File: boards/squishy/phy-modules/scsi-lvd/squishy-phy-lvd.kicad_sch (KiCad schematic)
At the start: 39 parts, among them J1 SCSI PHY Mezz, J2 SCSI Connector, J3 Conn_01x04, Q5 PMDPB58UPE,115, Q6 DMN65D8L-7, U1 M24C02-RMC, U21 LM321, U39 LM2903

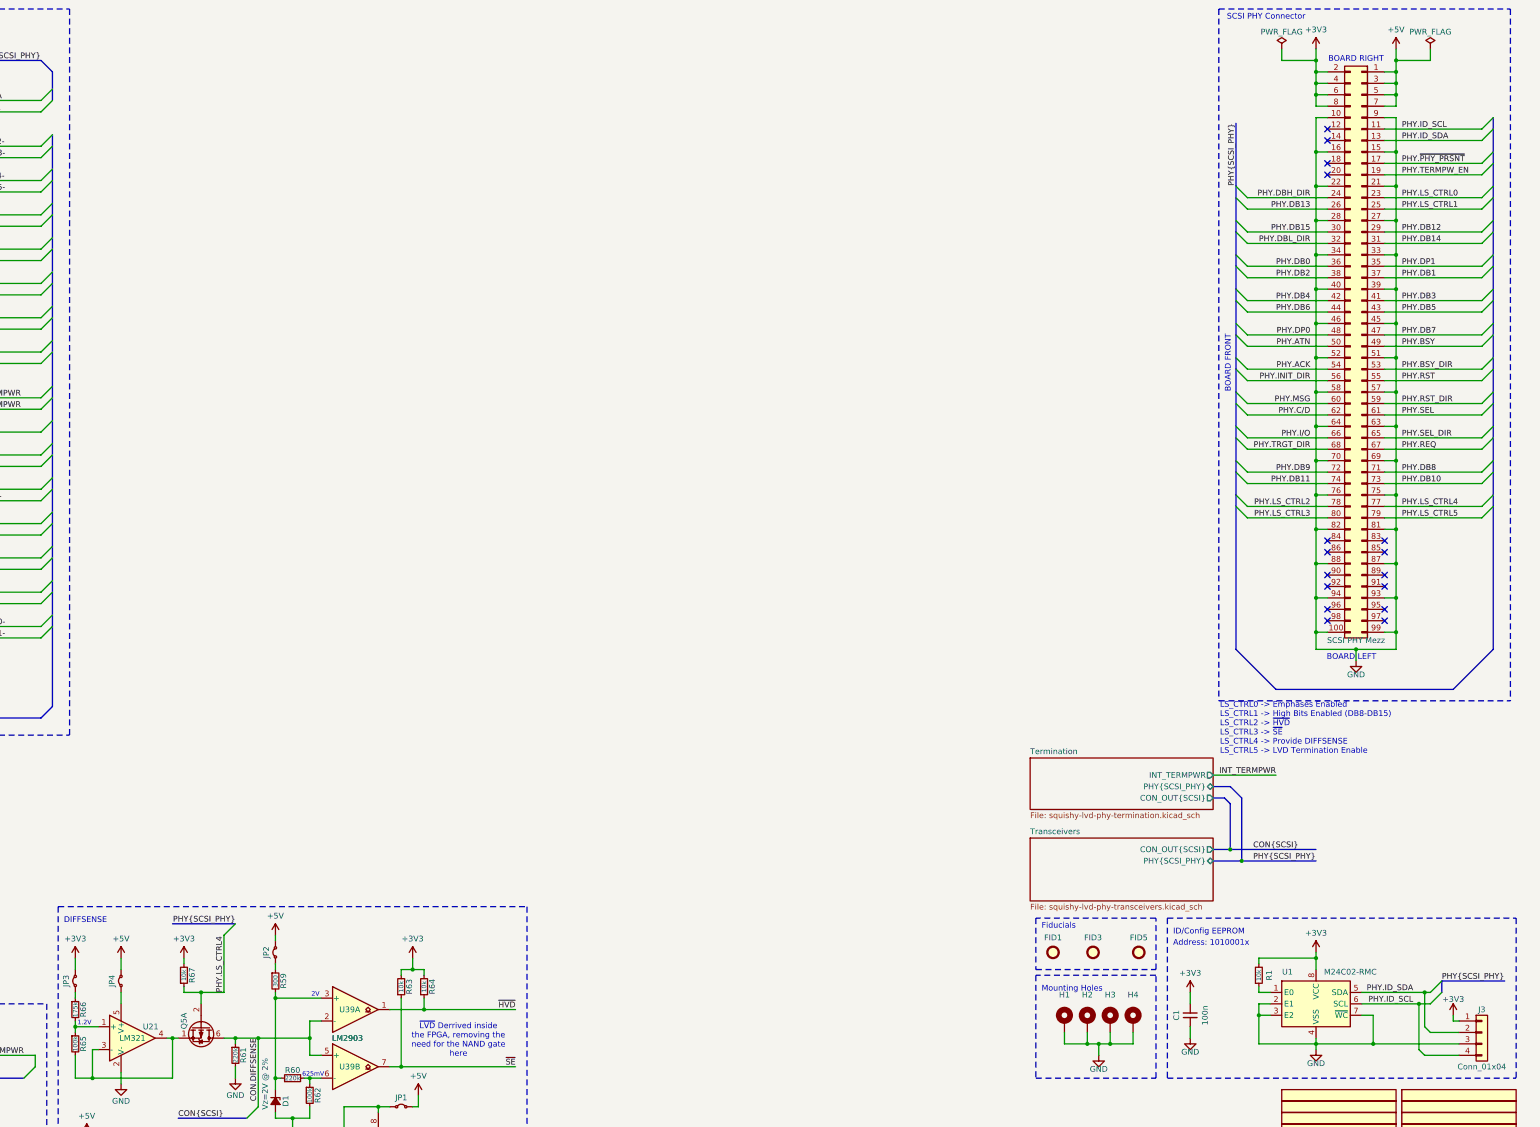
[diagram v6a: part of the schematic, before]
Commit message: squishy: phy: lvd: Started re-working the LVD PHY
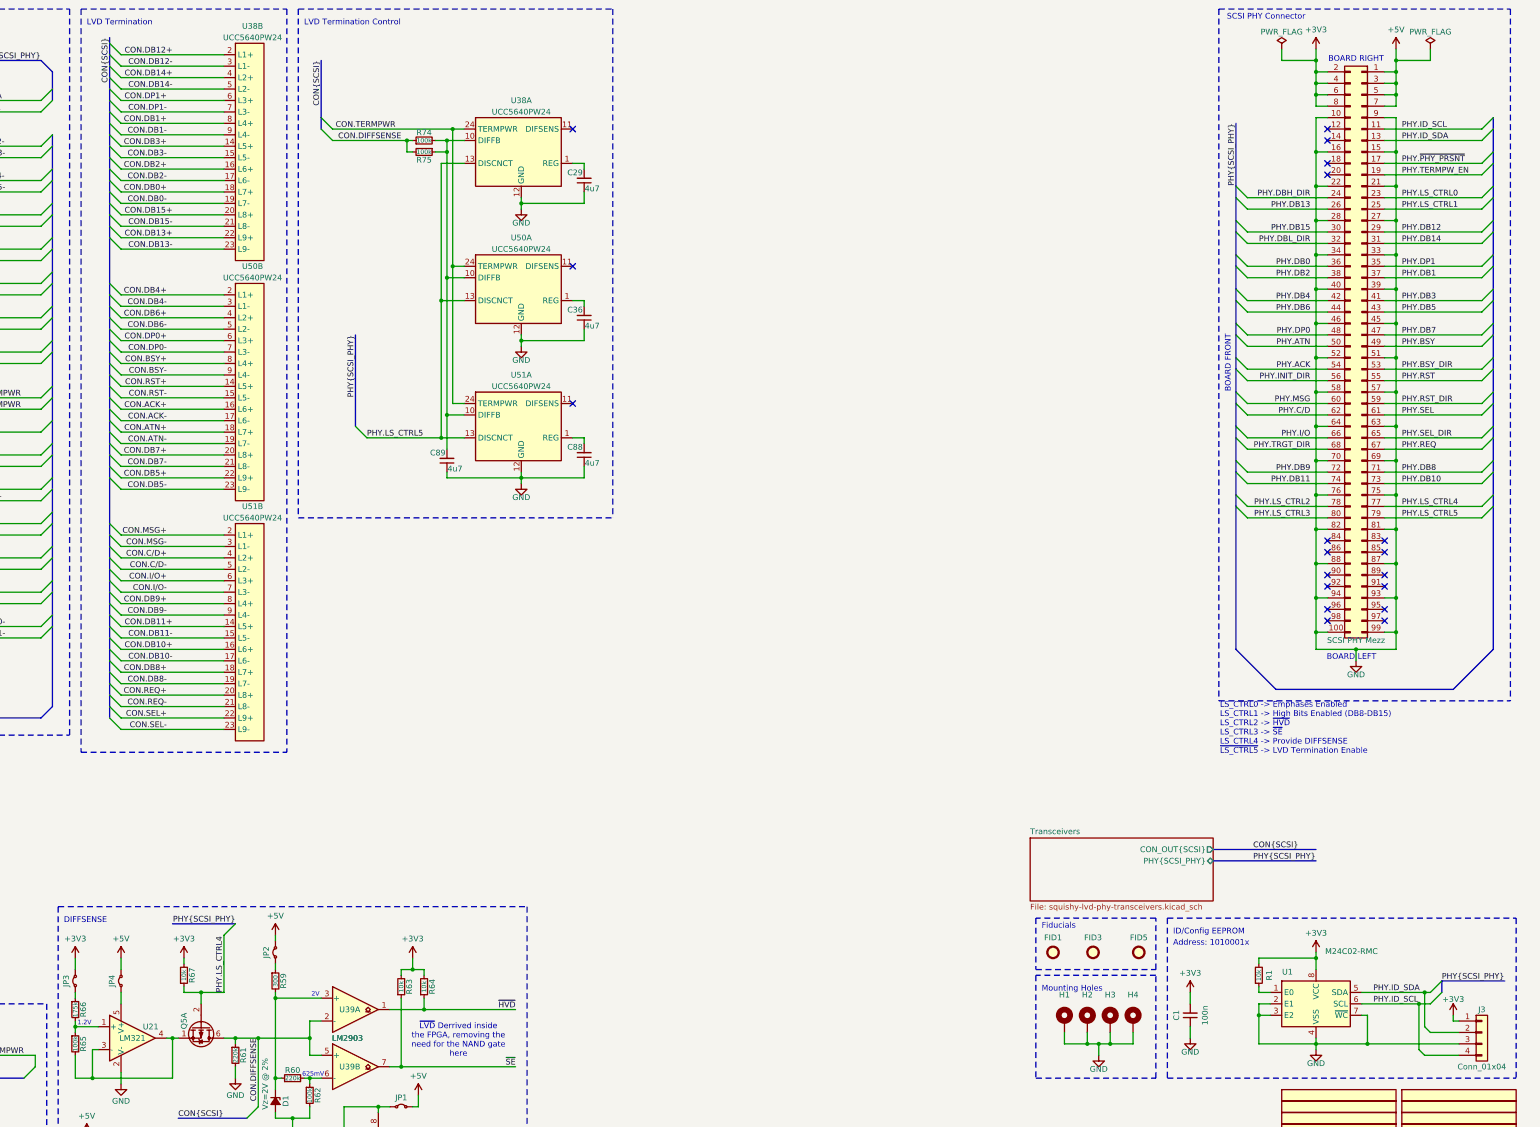
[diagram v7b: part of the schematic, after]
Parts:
- added C29, C36, C88, C89: 4u7, rhais_rcl:C0402, symbol Device:C_Small
- added R74, R75: 100k, rhais_rcl:R0402, symbol Device:R_Small
- added U38, U50, U51: UCC5640PW24, Package_SO:TSSOP-24_4.4x7.8mm_P0.65mm, symbol lethalbit-io:UCC5640PW24
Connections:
- net CON.ACK+: now also U50.16 (L6+)
- net CON.ACK-: now also U50.17 (L6-)
- net CON.ATN+: now also U50.18 (L7+)
- net CON.ATN-: now also U50.19 (L7-)
- net CON.BSY+: now also U50.8 (L4+)
- net CON.BSY-: now also U50.9 (L4-)
- net CON.C/D+: now also U51.4 (L2+)
- net CON.C/D-: now also U51.5 (L2-)
- net CON.DB0+: now also U38.18 (L7+)
- net CON.DB0-: now also U38.19 (L7-)
- net CON.DB1+: now also U38.8 (L4+)
- net CON.DB1-: now also U38.9 (L4-)
- net CON.DB10+: now also U51.16 (L6+)
- net CON.DB10-: now also U51.17 (L6-)
- net CON.DB11+: now also U51.14 (L5+)
- net CON.DB11-: now also U51.15 (L5-)
- net CON.DB13+: now also U38.22 (L9+)
- net CON.DB13-: now also U38.23 (L9-)
- net CON.DB15+: now also U38.20 (L8+)
- net CON.DB15-: now also U38.21 (L8-)
- net CON.DB2+: now also U38.16 (L6+)
- net CON.DB2-: now also U38.17 (L6-)
- net CON.DB3+: now also U38.14 (L5+)
- net CON.DB3-: now also U38.15 (L5-)
- net CON.DB4+: now also U50.2 (L1+)
- net CON.DB4-: now also U50.3 (L1-)
- net CON.DB5+: now also U50.22 (L9+)
- net CON.DB5-: now also U50.23 (L9-)
- net CON.DB6+: now also U50.4 (L2+)
- net CON.DB6-: now also U50.5 (L2-)
- net CON.DB7+: now also U50.20 (L8+)
- net CON.DB7-: now also U50.21 (L8-)
- net CON.DB8+: now also U51.18 (L7+)
- net CON.DB8-: now also U51.19 (L7-)
- net CON.DB9+: now also U51.8 (L4+)
- net CON.DB9-: now also U51.9 (L4-)
- net CON.DIFFSENSE: now also R74.1, R75.2
- net CON.DP0+: now also U50.6 (L3+)
- net CON.DP0-: now also U50.7 (L3-)
- net CON.DP1+: now also U38.6 (L3+)
- net CON.DP1-: now also U38.7 (L3-)
- net CON.I/O+: now also U51.6 (L3+)
- net CON.I/O-: now also U51.7 (L3-)
- net CON.MSG+: now also U51.2 (L1+)
- net CON.MSG-: now also U51.3 (L1-)
- net CON.REQ+: now also U51.20 (L8+)
- net CON.REQ-: now also U51.21 (L8-)
- net CON.RST+: now also U50.14 (L5+)
- net CON.RST-: now also U50.15 (L5-)
- net CON.SEL+: now also U51.22 (L9+)
- net CON.SEL-: now also U51.23 (L9-)
- net CON.TERMPWR: now also U38.24 (TERMPWR), U50.24 (TERMPWR), U51.24 (TERMPWR)
- net GND: now also C29.1, C36.1, C88.1, C89.1, U38.12 (GND), U50.12 (GND), U51.12 (GND)
- net PHY.LS_CTRL5: now also U38.13 (DISCNCT), U50.13 (DISCNCT), U51.13 (DISCNCT)
- new net: C88.2, U51.1 (REG)
- new net: C36.2, U50.1 (REG)
- new net: C29.2, U38.1 (REG)
- new net: C89.2, R74.2, R75.1, U38.10 (DIFFB), U50.10 (DIFFB), U51.10 (DIFFB)
- new net CON.DB12+: U38.2 (L1+)
- new net CON.DB12-: U38.3 (L1-)
- new net CON.DB14+: U38.4 (L2+)
- new net CON.DB14-: U38.5 (L2-)
- no-connect marks 18 -> 21
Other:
- removed sheet Termination
- note added: "LS_CTRL0 -> Emphases Enabled LS_CTRL1 -> High Bits Enabled (DB8-DB15) LS_CTRL2 -> ~{HVD} LS_CTRL3 -> ~{SE} LS_CTRL4 -> Provide DIFFSENSE ~{LS_CTRL5} -> LVD Termination Enable"
- note added: "LVD Termination"
- note added: "LVD Termination Control"
- note removed: "LS_CTRL0 -> Emphases Enabled LS_CTRL1 -> High Bits Enabled (DB8-DB15) LS_CTRL2 -> ~{HVD} LS_CTRL3 -> ~{SE} LS_CTRL4 -> Provide DIFFSENSE LS_CTRL5 -> LVD Termination Enable"

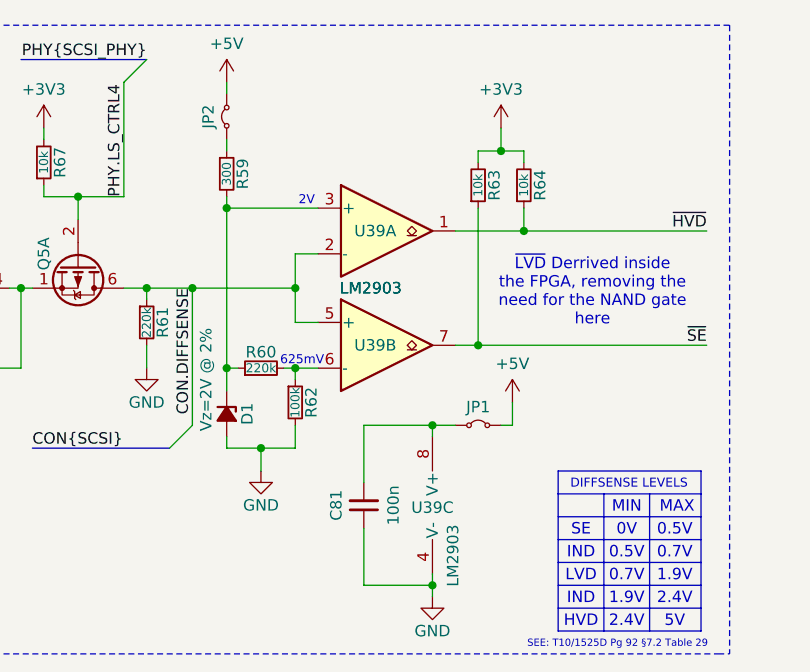
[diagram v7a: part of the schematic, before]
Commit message: squishy:  phy: lvd: Upgraded to KiCad v9
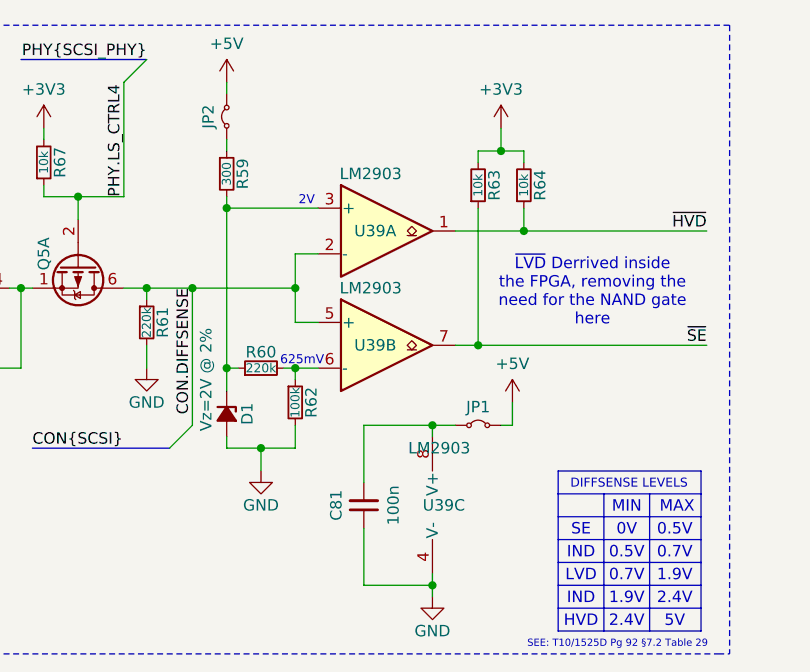
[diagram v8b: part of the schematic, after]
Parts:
- C1, C81, C86: footprint rhais_rcl:C0603 -> rhais_rcl:C0402
- R1, R63, R64, R67, R68, R69, R70, R71: footprint rhais_rcl:R0603 -> rhais_rcl:R0402
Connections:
- net GND: now also U39.9 (V-)
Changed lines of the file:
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@@
 			)
 		)
-		(property "Footprint" "rhais_rcl:C0603"
+		(property "Footprint" "rhais_rcl:C0402"
 			(at 334.01 237.49 0)
 			(effects
@@
 	)
 	(symbol
+		(lib_name "LM2903_2")
 		(lib_id "Comparator:LM2903")
 		(at 156.21 266.7 0)
@@
 		(dnp no)
 		(property "Reference" "U39"
-			(at 153.67 266.954 0)
+			(at 154.94 266.7 0)
 			(effects
 				(font
@@
 		)
 		(property "Value" "LM2903"
-			(at 155.956 272.288 90)
+			(at 154.432 260.35 0)
 			(effects
 				(font
@@
 		(pin "8"
 		)
+		(pin "9"
+		)
 		(instances
 			(project ""
@@
 			)
 		)
-		(property "Footprint" "rhais_rcl:R0603"
+		(property "Footprint" "rhais_rcl:R0402"
 			(at 40.64 267.97 0)
 			(effects
@@
 			)
 		)
-		(property "Footprint" "rhais_rcl:R0603"
+		(property "Footprint" "rhais_rcl:R0402"
 			(at 158.75 231.14 0)
 			(effects
@@
 			)
 		)
-		(property "Footprint" "rhais_rcl:R0603"
+		(property "Footprint" "rhais_rcl:R0402"
 			(at 35.56 262.89 0)
 			(effects
@@
 			)
 		)
-		(property "Footprint" "rhais_rcl:R0603"
+		(property "Footprint" "rhais_rcl:R0402"
 			(at 48.26 257.81 0)
 			(effects
@@
 			)
 		)
-		(property "Footprint" "rhais_rcl:R0603"
+		(property "Footprint" "rhais_rcl:R0402"
 			(at 55.88 257.81 0)
 			(effects
@@
 			)
 		)
-		(property "Footprint" "rhais_rcl:C0603"
+		(property "Footprint" "rhais_rcl:C0402"
 			(at 146.05 266.7 0)
 			(effects
@@
 	)
 	(symbol
+		(lib_name "LM2903_1")
 		(lib_id "Comparator:LM2903")
 		(at 148.59 236.22 0)
@@
 		)
 		(property "Value" "LM2903"
-			(at 146.812 242.57 0)
+			(at 146.812 229.87 0)
 			(effects
 				(font
@@
 		(pin "8"
 		)
+		(pin "9"
+		)
 		(instances
 			(project ""
@@
 			)
 		)
-		(property "Footprint" "rhais_rcl:R0603"
+		(property "Footprint" "rhais_rcl:R0402"
 			(at 349.25 228.6 0)
 			(effects
@@
 			)
 		)
-		(property "Footprint" "rhais_rcl:R0603"
+		(property "Footprint" "rhais_rcl:R0402"
 			(at 163.83 231.14 0)
 			(effects
@@
 			)
 		)
-		(property "Footprint" "rhais_rcl:R0603"
+		(property "Footprint" "rhais_rcl:R0402"
 			(at 110.49 228.6 0)
 			(effects
@@
 			)
 		)
-		(property "Footprint" "rhais_rcl:C0603"
+		(property "Footprint" "rhais_rcl:C0402"
 			(at 88.9 267.97 0)
 			(effects
@@
 		(pin "8"
 		)
+		(pin "9"
+		)
 		(instances
